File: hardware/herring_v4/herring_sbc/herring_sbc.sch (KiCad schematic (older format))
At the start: 2 parts

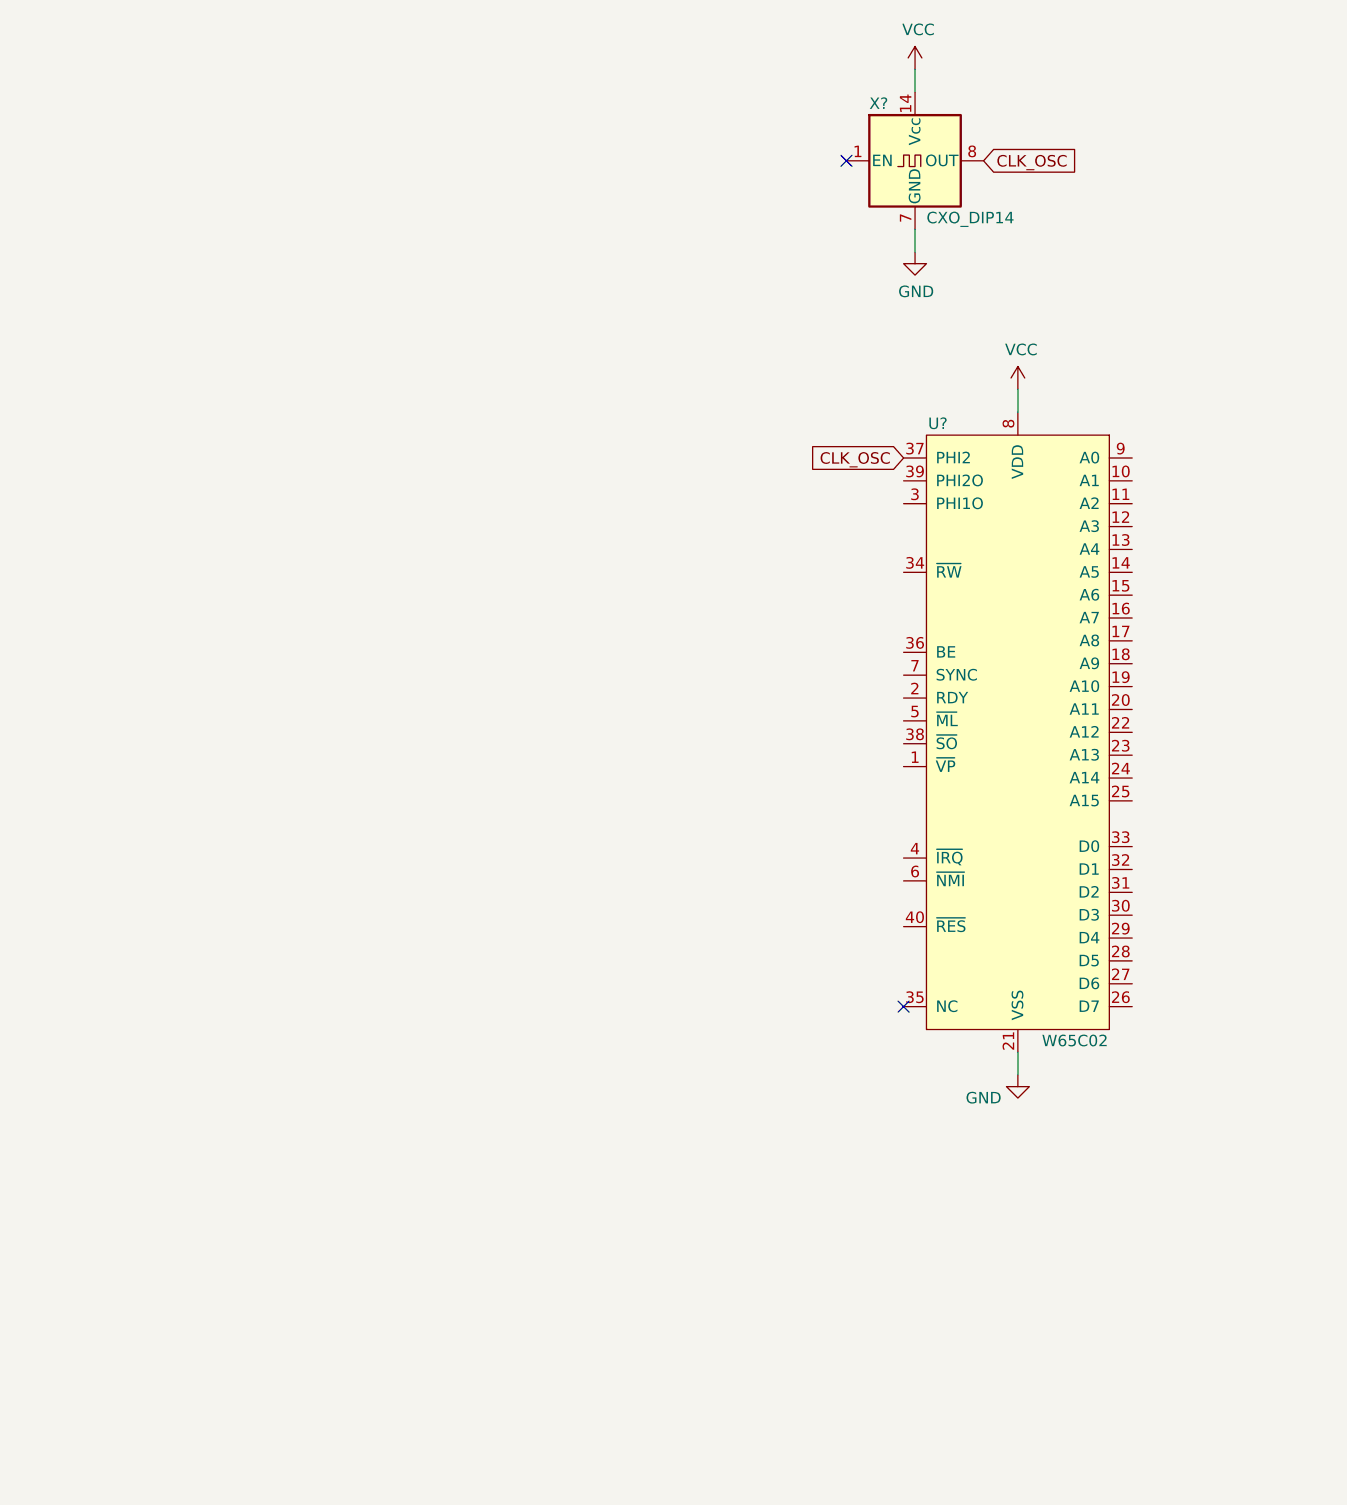
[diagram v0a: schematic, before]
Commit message: Add 16C550 symbol
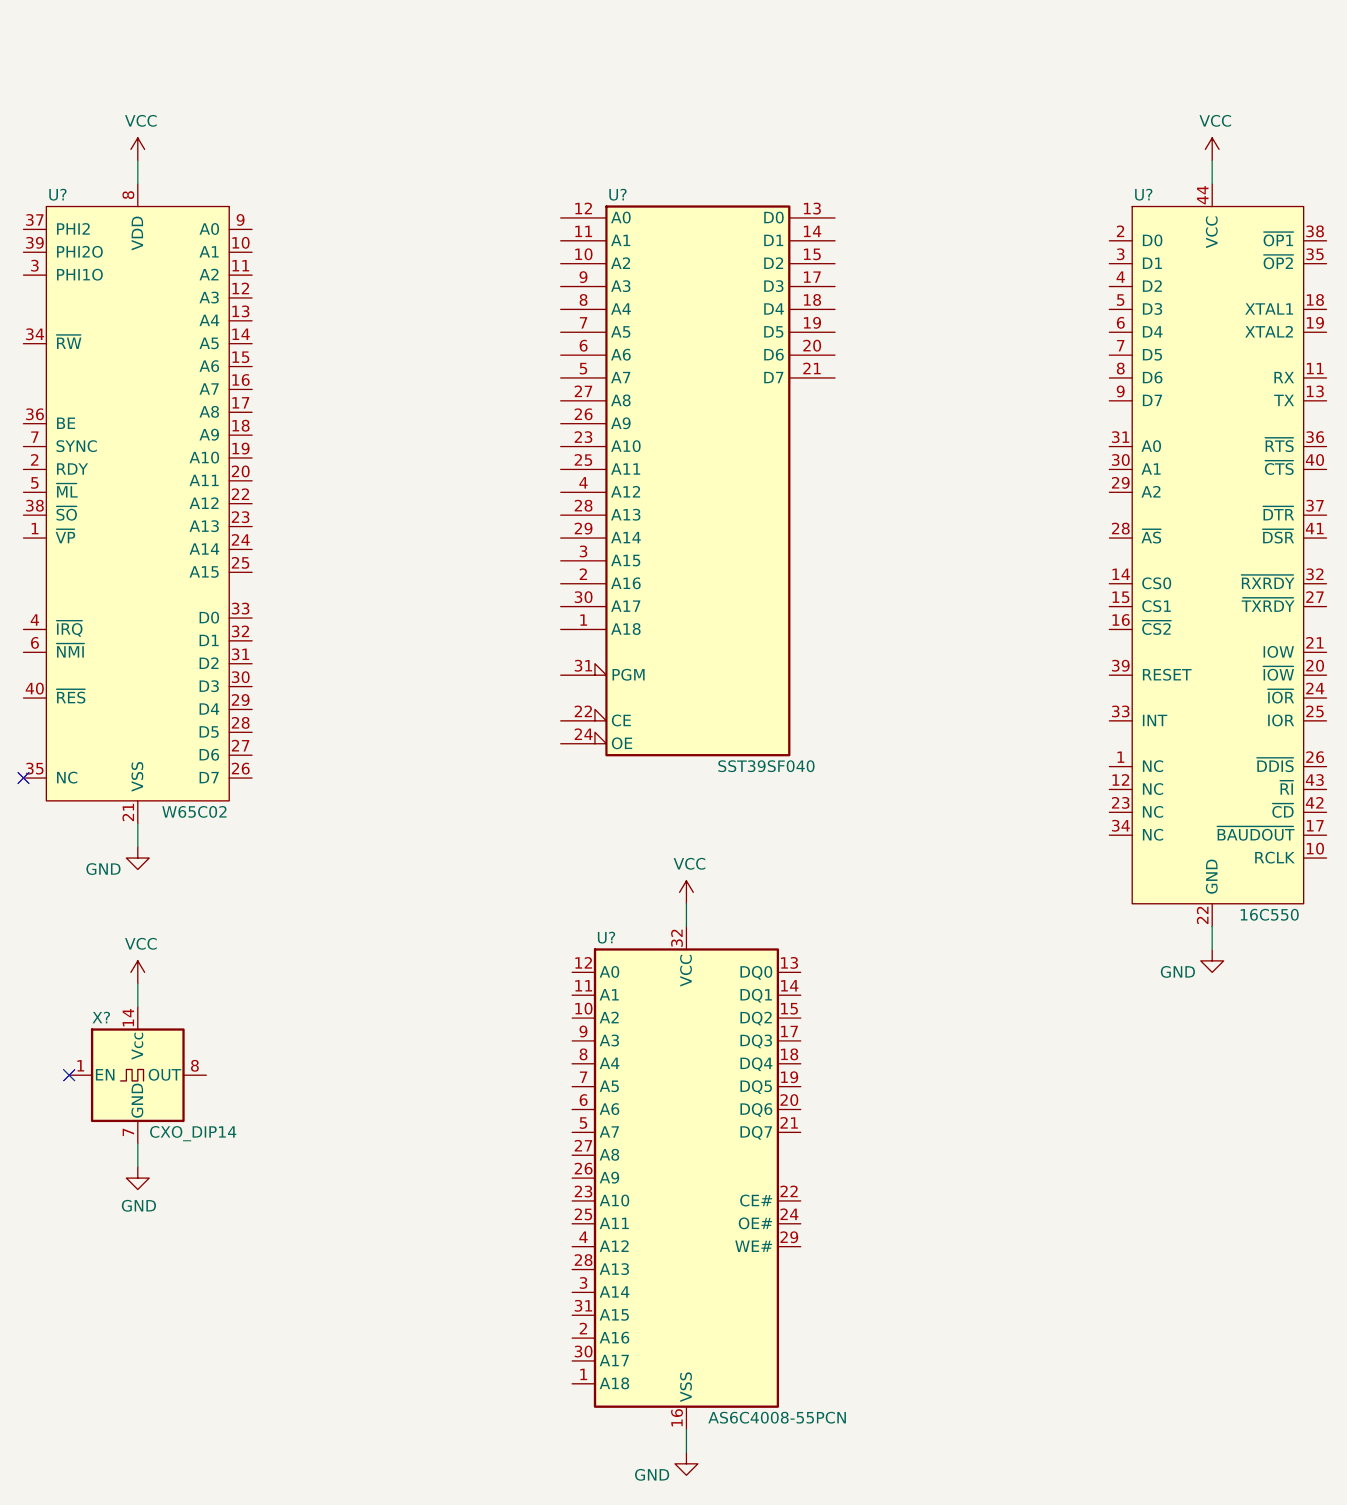
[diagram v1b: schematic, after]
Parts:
- added U?: SST39SF040, symbol Memory_Flash:SST39SF040
- added U?: AS6C4008-55PCN, Package_DIP:DIP-32_W15.24mm, symbol Memory_RAM:AS6C4008-55PCN
- added U?: 16C550, symbol herring:16C550
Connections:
- net GND: now also U?.16 (GND), U?.16 (VSS), U?.22 (GND)
- net VCC: now also U?.32 (VCC), U?.32 (VCC), U?.44 (VCC)
- net CLK_OSC: no longer names the net of U?.37 (PHI2)
- net CLK_OSC: no longer X?.8 (OUT)
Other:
- moved on the sheet: U?, X?
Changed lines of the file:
@@
 L herring:W65C02 U?
 U 1 1 634E5D35
-P 5750 3800
-F 0 "U?" H 5400 5150 50  0000 C CNN
-F 1 "W65C02" H 6000 2450 50  0000 C CNN
-F 2 "" H 5750 3800 50  0001 C CNN
-F 3 "" H 5750 3800 50  0001 C CNN
-	1    5750 3800
+P 1900 2800
+F 0 "U?" H 1550 4150 50  0000 C CNN
+F 1 "W65C02" H 2150 1450 50  0000 C CNN
+F 2 "" H 1900 2800 50  0001 C CNN
+F 3 "" H 1900 2800 50  0001 C CNN
+	1    1900 2800
 	1    0    0    -1
 $EndComp
@@
 L Oscillator:CXO_DIP14 X?
 U 1 1 634EC20A
-P 5300 1300
-F 0 "X?" H 5100 1550 50  0000 L CNN
-F 1 "CXO_DIP14" H 5350 1050 50  0000 L CNN
-F 2 "Oscillator:Oscillator_DIP-14" H 5750 950 50  0001 C CNN
-F 3 "http://cdn-reichelt.de/documents/datenblatt/B400/OSZI.pdf" H 5200 1300 50  0001 C CNN
-	1    5300 1300
+P 1900 5300
+F 0 "X?" H 1700 5550 50  0000 L CNN
+F 1 "CXO_DIP14" H 1950 5050 50  0000 L CNN
+F 2 "Oscillator:Oscillator_DIP-14" H 2350 4950 50  0001 C CNN
+F 3 "http://cdn-reichelt.de/documents/datenblatt/B400/OSZI.pdf" H 1800 5300 50  0001 C CNN
+	1    1900 5300
 	1    0    0    -1
 $EndComp
-NoConn ~ 5250 5000
+NoConn ~ 1400 4000
 $Comp
 L power:VCC #PWR?
 U 1 1 634F0394
-P 5750 2300
-F 0 "#PWR?" H 5750 2150 50  0001 C CNN
-F 1 "VCC" H 5765 2473 50  0000 C CNN
-F 2 "" H 5750 2300 50  0001 C CNN
-F 3 "" H 5750 2300 50  0001 C CNN
-	1    5750 2300
+P 1900 1300
+F 0 "#PWR?" H 1900 1150 50  0001 C CNN
+F 1 "VCC" H 1915 1473 50  0000 C CNN
+F 2 "" H 1900 1300 50  0001 C CNN
+F 3 "" H 1900 1300 50  0001 C CNN
+	1    1900 1300
 	1    0    0    -1
 $EndComp
@@
 L power:VCC #PWR?
 U 1 1 634F1077
-P 5300 900
-F 0 "#PWR?" H 5300 750 50  0001 C CNN
-F 1 "VCC" H 5315 1073 50  0000 C CNN
-F 2 "" H 5300 900 50  0001 C CNN
-F 3 "" H 5300 900 50  0001 C CNN
-	1    5300 900
+P 1900 4900
+F 0 "#PWR?" H 1900 4750 50  0001 C CNN
+F 1 "VCC" H 1915 5073 50  0000 C CNN
+F 2 "" H 1900 4900 50  0001 C CNN
+F 3 "" H 1900 4900 50  0001 C CNN
+	1    1900 4900
 	1    0    0    -1
 $EndComp
@@
 L power:GND #PWR?
 U 1 1 634F25BA
-P 5300 1700
-F 0 "#PWR?" H 5300 1450 50  0001 C CNN
-F 1 "GND" H 5305 1527 50  0000 C CNN
-F 2 "" H 5300 1700 50  0001 C CNN
-F 3 "" H 5300 1700 50  0001 C CNN
-	1    5300 1700
+P 1900 5700
+F 0 "#PWR?" H 1900 5450 50  0001 C CNN
+F 1 "GND" H 1905 5527 50  0000 C CNN
+F 2 "" H 1900 5700 50  0001 C CNN
+F 3 "" H 1900 5700 50  0001 C CNN
+	1    1900 5700
 	1    0    0    -1
 $EndComp
@@
 L power:GND #PWR?
 U 1 1 634F3310
-P 5750 5300
-F 0 "#PWR?" H 5750 5050 50  0001 C CNN
-F 1 "GND" H 5600 5200 50  0000 C CNN
-F 2 "" H 5750 5300 50  0001 C CNN
-F 3 "" H 5750 5300 50  0001 C CNN
-	1    5750 5300
+P 1900 4300
+F 0 "#PWR?" H 1900 4050 50  0001 C CNN
+F 1 "GND" H 1750 4200 50  0000 C CNN
+F 2 "" H 1900 4300 50  0001 C CNN
+F 3 "" H 1900 4300 50  0001 C CNN
+	1    1900 4300
 	1    0    0    -1
 $EndComp
 Wire Wire Line
-	5300 1600 5300 1700
+	1900 5600 1900 5700
 Wire Wire Line
-	5300 900  5300 1000
+	1900 4900 1900 5000
 Wire Wire Line
-	5750 2300 5750 2400
+	1900 1300 1900 1400
 Wire Wire Line
-	5750 5200 5750 5300
-NoConn ~ 5000 1300
-Text GLabel 5600 1300 2    50   Input ~ 0
-CLK_OSC
-Text GLabel 5250 2600 0    50   Input ~ 0
-CLK_OSC
+	1900 4200 1900 4300
+NoConn ~ 1600 5300
+$Comp
+L Memory_Flash:SST39SF040 U?
+U 1 1 6350D23C
+P 4350 2750
+F 0 "U?" H 4000 4050 50  0000 C CNN
+F 1 "SST39SF040" H 4650 1550 50  0000 C CNN
+F 2 "" H 4350 3050 50  0001 C CNN
+F 3 "http://ww1.microchip.com/downloads/en/DeviceDoc/25022B.pdf" H 4350 3050 50  0001 C CNN
+	1    4350 2750
+	1    0    0    -1
+$EndComp
+$Comp
+L Memory_RAM:AS6C4008-55PCN U?
+U 1 1 63519481
+P 4300 5750
+F 0 "U?" H 3950 6800 50  0000 C CNN
+F 1 "AS6C4008-55PCN" H 4700 4700 50  0000 C CNN
+F 2 "Package_DIP:DIP-32_W15.24mm" H 4300 5850 50  0001 C CNN
+F 3 "https://www.alliancememory.com/wp-content/uploads/pdf/AS6C4008.pdf" H 4300 5850 50  0001 C CNN
+	1    4300 5750
+	1    0    0    -1
+$EndComp
+$Comp
+L power:GND #PWR?
+U 1 1 6351D3F6
+P 4300 6950
+F 0 "#PWR?" H 4300 6700 50  0001 C CNN
+F 1 "GND" H 4150 6850 50  0000 C CNN
+F 2 "" H 4300 6950 50  0001 C CNN
+F 3 "" H 4300 6950 50  0001 C CNN
+	1    4300 6950
+	1    0    0    -1
+$EndComp
+Wire Wire Line
+	4300 6850 4300 6950
+$Comp
+L power:VCC #PWR?
+U 1 1 6351EEC5
+P 4300 4550
+F 0 "#PWR?" H 4300 4400 50  0001 C CNN
+F 1 "VCC" H 4315 4723 50  0000 C CNN
+F 2 "" H 4300 4550 50  0001 C CNN
+F 3 "" H 4300 4550 50  0001 C CNN
+	1    4300 4550
+	1    0    0    -1
+$EndComp
+Wire Wire Line
+	4300 4550 4300 4650
+$Comp
+L herring:16C550 U?
+U 1 1 63532C2A
+P 6600 3000
+F 0 "U?" H 6300 4550 50  0000 C CNN
+F 1 "16C550" H 6850 1400 50  0000 C CNN
+F 2 "" H 6400 3750 50  0001 C CNN
+F 3 "" H 6400 3750 50  0001 C CNN
+	1    6600 3000
+	1    0    0    -1
+$EndComp
+$Comp
+L power:VCC #PWR?
+U 1 1 635365C9
+P 6600 1300
+F 0 "#PWR?" H 6600 1150 50  0001 C CNN
+F 1 "VCC" H 6615 1473 50  0000 C CNN
+F 2 "" H 6600 1300 50  0001 C CNN
+F 3 "" H 6600 1300 50  0001 C CNN
+	1    6600 1300
+	1    0    0    -1
+$EndComp
+Wire Wire Line
+	6600 1300 6600 1400
+$Comp
+L power:GND #PWR?
+U 1 1 63537B82
+P 6600 4750
+F 0 "#PWR?" H 6600 4500 50  0001 C CNN
+F 1 "GND" H 6450 4650 50  0000 C CNN
+F 2 "" H 6600 4750 50  0001 C CNN
+F 3 "" H 6600 4750 50  0001 C CNN
+	1    6600 4750
+	1    0    0    -1
+$EndComp
+Wire Wire Line
+	6600 4650 6600 4750
 $EndSCHEMATC
